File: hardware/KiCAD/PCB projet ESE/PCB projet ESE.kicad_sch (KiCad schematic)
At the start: 46 parts, among them J1 Conn_01x06, J16 Conn_01x03, J2 Conn_01x04, J3 Conn_01x06, J4 Conn_01x06, J5 Conn_01x04, J6 Conn_01x02, J7 Conn_ST_STDC14, SW1 SW_SPST, SW2 472121010111, U1 ZXBM5210-SP, U2 ZXBM5210-SP, U3 STM32G474RETx, U4 ADXL343

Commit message: v1 PCB
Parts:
- removed J3: Conn_01x06, Connector_JST:JST_SH_BM06B-SRSS-TB_1x06-1MP_P1.00mm_Vertical, symbol Connector_Generic:Conn_01x06
- added C5: 100n, Capacitor_SMD:C_0402_1005Metric, symbol Device:C_Small
- added C7: 10u, Capacitor_SMD:C_0402_1005Metric, symbol Device:C_Small
- added D1: D_TVS_Small, Diode_SMD:D_SOD-523, symbol Device:D_TVS_Small
- added F1: 3.3A, Fuse:Fuse_2920_7451Metric, symbol Device:Polyfuse_Small
- added J5: Conn_01x02, Connector_JST:JST_XH_B2B-XH-A_1x02_P2.50mm_Vertical, symbol Connector_Generic:Conn_01x02
- added J6: Conn_01x02, Connector_JST:JST_SH_BM02B-SRSS-TB_1x02-1MP_P1.00mm_Vertical, symbol Connector_Generic:Conn_01x02
- added TP1, TP2, TP3, TP4, TP5, TP6: TestPoint, TestPoint:TestPoint_Pad_D1.0mm, symbol Connector:TestPoint
- renumbered C8 to C10, C9 to C11, C10 to C12, C11 to C13, C12 to C14, C13 to C15, C14 to C16, C15 to C17, C16 to C18, C17 to C19, C5 to C6, C6 to C8, C7 to C9, D1 to D2, D2 to D3, D3 to D4, J4 to J3, J16 to J4, J5 to J7, J6 to J8, J7 to J9, R3 to R2, R4 to R3, R2 to R4
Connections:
- net INT_7 is gone; now on net INT_5: U3.34 (PB12)
- net INT_8 is gone; now on net Lidar Output : U3.35 (PB13)
- net XSHUT_7 is gone; now on net XSHUT_5: U3.33 (PB11)
- net +5V: now also F1.2
- net Accel SCL: now also TP4.1
- net Accel SDA: now also TP5.1
- net Encodeur_A_Phase_1: now also U3.9 (PC1); no longer U3.8 (PC0)
- net Encodeur_B_Phase_1: now also U3.8 (PC0); no longer U3.9 (PC1)
- net GND: now also C5.2, C7.2, D1.1 (A1), J5.1 (Pin_1)
- net INT_5: no longer U3.37 (PB15)
- net Lidar Output : no longer U3.3 (PC14)
- net PWM FWD 1: now also TP6.1
- net PWM FWD 2: now also TP2.1
- net PWM REV 1: now also TP3.1
- net PWM REV 2: now also TP1.1
- net XSHUT_5: no longer U3.44 (PA10)
- net PG_52: no longer names the net of U3.51 (PA15)
- net UART_HC05_RX renamed UART_PIi_Zero_RX
- net UART_PIi_Zero_RX: now also J6.2 (Pin_2)
- net UART_HC05_TX renamed UART_Pi_Zero_TX
- net UART_Pi_Zero_TX: now also J6.1 (Pin_1)
- net XSHUT_8: no longer names the net of U3.36 (PB14)
- new net: C5.1, C7.1, D1.2 (A2), F1.1, J5.2 (Pin_2)
- no-connect marks 17 -> 20
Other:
- removed sheet Rasbpi
- sheet Régulateurs ports: added none; removed PG_52
- sheet TOF ports: added none; removed INT 7, INT 8, XSHUT_7, XSHUT_8
- note added: "Rasbpi JST XH 3A max"

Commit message: maj pcb and pinout
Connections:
- net UART_PIi_Zero_RX renamed UART_Pi_Zero_RX
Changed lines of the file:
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@@
 		)
 	)
-	(global_label "UART_PIi_Zero_RX"
+	(global_label "UART_Pi_Zero_RX"
 		(shape input)
 		(at 100.33 119.38 0)
@@
 		)
 		(property "Intersheetrefs" "${INTERSHEET_REFS}"
-			(at 120.5431 119.38 0)
+			(at 119.9383 119.38 0)
 			(effects
 				(font
@@
 		)
 	)
-	(global_label "UART_PIi_Zero_RX"
+	(global_label "UART_Pi_Zero_RX"
 		(shape input)
 		(at 165.1 45.72 0)
@@
 		)
 		(property "Intersheetrefs" "${INTERSHEET_REFS}"
-			(at 185.3131 45.72 0)
+			(at 184.7083 45.72 0)
 			(effects
 				(font

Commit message: update
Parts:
- removed C5: 100n, Capacitor_SMD:C_0402_1005Metric, symbol Device:C_Small
- removed C7: 10u, Capacitor_SMD:C_0402_1005Metric, symbol Device:C_Small
- removed D1: D_TVS_Small, Diode_SMD:D_SOD-523, symbol Device:D_TVS_Small
- removed F1: 3.3A, Fuse:Fuse_2920_7451Metric, symbol Device:Polyfuse_Small
- removed J5: Conn_01x02, Connector_JST:JST_XH_B2B-XH-A_1x02_P2.50mm_Vertical, symbol Connector_Generic:Conn_01x02
- removed J6: Conn_01x02, Connector_JST:JST_SH_BM02B-SRSS-TB_1x02-1MP_P1.00mm_Vertical, symbol Connector_Generic:Conn_01x02
- added C29: 100n, Capacitor_SMD:C_0402_1005Metric, symbol Device:C_Small
- added C30: 10u, Capacitor_SMD:C_0603_1608Metric, symbol Device:C_Small
- added D5: D_TVS_Small, Diode_SMD:D_SOD-523, symbol Device:D_TVS_Small
- added F2: 3.3A, Fuse:Fuse_2920_7451Metric, symbol Device:Polyfuse_Small
- added J16: Conn_01x04, Connector_JST:JST_PH_B4B-PH-K_1x04_P2.00mm_Vertical, symbol Connector_Generic:Conn_01x04
- J1, J3: footprint Connector_JST:JST_PH_B6B-PH-K_1x06_P2.00mm_Vertical -> Connector_JST:JST_PH_S6B-PH-K_1x06_P2.00mm_Horizontal
- R2: value 18k -> 20k
- R3: value 10k -> 5k6
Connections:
- net +5V: now also F2.2
- net GND: now also C29.2, C30.2, D5.1 (A1), J16.1 (Pin_1)
- net UART_Pi_Zero_RX: now also J16.3 (Pin_3)
- net UART_Pi_Zero_TX: now also J16.4 (Pin_4)
- new net: C29.1, C30.1, D5.2 (A2), F2.1, J16.2 (Pin_2)
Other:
- note added: "1.65V"
- note added: "Rasbpi JST PH 1A max"
- note removed: "2.6V"
- note removed: "Rasbpi JST XH 3A max"
- moved on the sheet: J7

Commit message: BOM
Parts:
- C19: value 0.1u -> 100n
- C3, C4: value 4.7u -> 4u7
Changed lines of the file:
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@@
 			)
 		)
-		(property "Value" "4.7u"
+		(property "Value" "4u7"
 			(at 48.2535 60.96 0)
 			(effects
@@
 			)
 		)
-		(property "Value" "4.7u"
+		(property "Value" "4u7"
 			(at 46.9835 21.59 0)
 			(effects
@@
 			)
 		)
-		(property "Value" "0.1u"
+		(property "Value" "100n"
 			(at 262.8963 22.86 90)
 			(effects

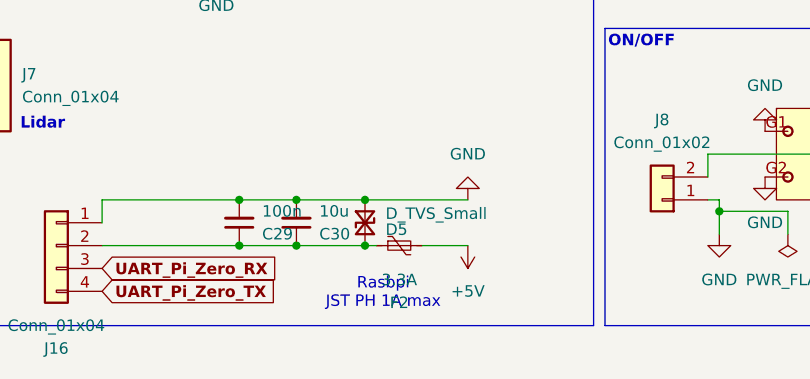
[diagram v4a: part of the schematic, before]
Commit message: maj mpn & gitignore
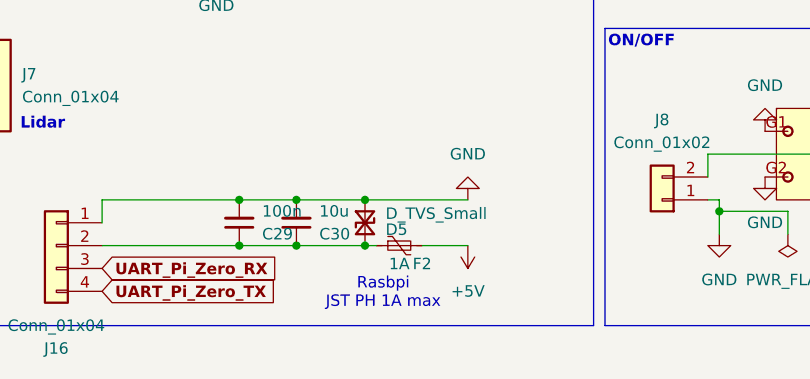
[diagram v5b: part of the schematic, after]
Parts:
- D5: MPN VESD01C1-02V-G3-08 -> VESD05A1-02V-G3-08
- F2: value 3.3A -> 1A
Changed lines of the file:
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@@
 			)
 		)
-		(property "Datasheet" "https://www.vishay.com/docs/86130/vesd01c1-02vtovesd33c1-02v.pdf"
+		(property "Datasheet" "https://www.vishay.com/docs/86129/vesd05a1-02v.pdf"
 			(at 102.87 184.15 0)
 			(effects
@@
 			)
 		)
-		(property "MPN" "VESD01C1-02V-G3-08 "
+		(property "MPN" "VESD05A1-02V-G3-08"
 			(at 102.87 184.15 90)
 			(effects
@@
 		(on_board yes)
 		(dnp no)
-		(fields_autoplaced yes)
 		(property "Reference" "F2"
-			(at 106.68 193.04 90)
-			(effects
-				(font
-					(size 1.27 1.27)
-				)
-			)
-		)
-		(property "Value" "3.3A"
-			(at 106.68 190.5 90)
-			(effects
-				(font
+			(at 109.22 188.722 90)
+			(effects
+				(font
+					(size 1.27 1.27)
+				)
+			)
+		)
+		(property "Value" "1A"
+			(at 106.68 188.722 90)
+			(effects
+				(font
